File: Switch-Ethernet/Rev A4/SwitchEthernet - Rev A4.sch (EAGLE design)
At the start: 109 parts, among them J1 22-05-7028-02, J2 DF17(2.0)-20DP-0.5V(57), J3 DF17(4.0)-20DP-0.5V(57), J4 22-05-7058-05, P1 RB1-125BAG1A, T1 H1102FNL, T2 H1102FNL, U1 TC1264-3.3, U2 TC1264-1.8, U3 KSZ8995MA, U4 AT24C02C-SSHM-B, X1 NE8FAV, X2 NE8FAV, Y1 8Z-25.000MHZMAAJ-T

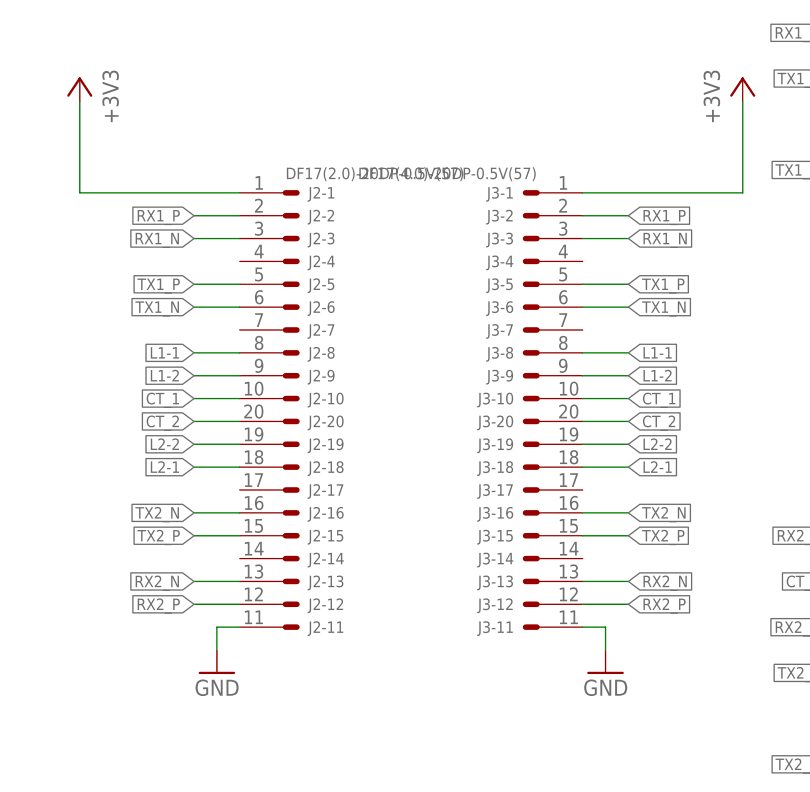
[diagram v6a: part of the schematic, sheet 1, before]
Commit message: Replace J2 to femal connector and reroute the board, replace holes
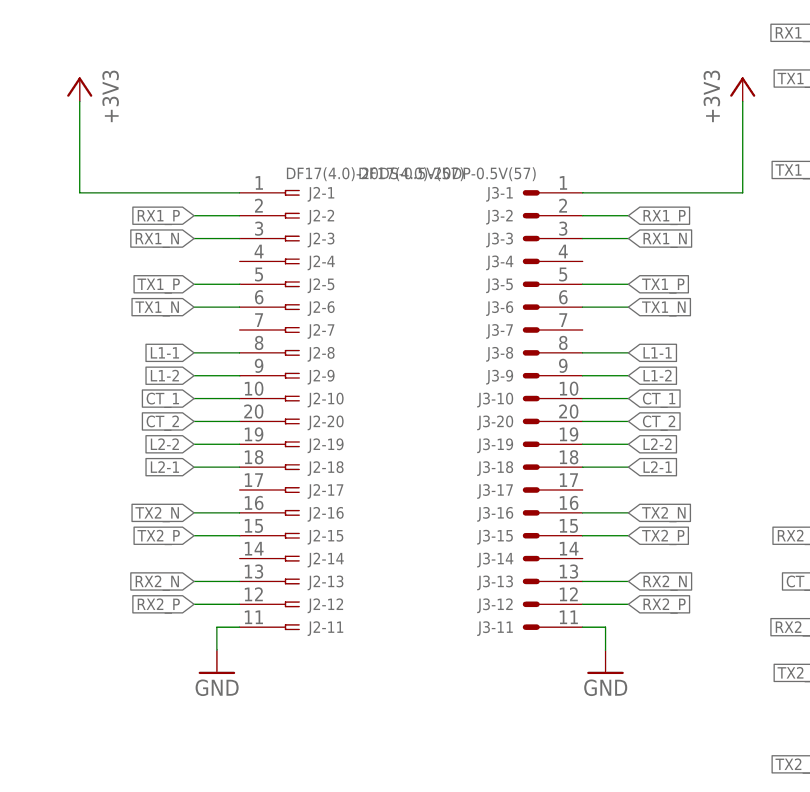
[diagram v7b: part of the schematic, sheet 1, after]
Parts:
- J2: value DF17(2.0)-20DP-0.5V(57) -> DF17(4.0)-20DS-0.5V(57); device con-hirose:DF17(2.0)-20DP-0.5V(57) -> con-hirose:DF17(4.0)-20DS-0.5V(57)
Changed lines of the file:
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@@
 <part name="+3V12" library="supply1" deviceset="+3V3" device=""/>
 <part name="+3V16" library="supply1" deviceset="+3V3" device=""/>
-<part name="J2" library="con-hirose" deviceset="DF17(?)-20DP-0.5V(57)" device="2.0"/>
+<part name="J2" library="con-hirose" deviceset="DF17(?)-20DS-0.5V(57)" device="4.0"/>
 <part name="J3" library="con-hirose" deviceset="DF17(?)-20DP-0.5V(57)" device="4.0"/>
 <part name="J4" library="con-molex" deviceset="22-?-05" device="05-7058"/>

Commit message: Modified the board according to the review
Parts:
- removed C40, C43, C44: 0.1uF, rcl:C-EUC0603
- removed C46, C47: 1000pF, 2kV, rcl:C-EUC1206
- removed J4: 22-05-7058-05, con-molex:22-05-7058-05
- removed LED7: Blue, led:LEDCHIP-LED0603
- removed R44: 1k, rcl:R-EU_R0603
- removed R45, R46: 49.9, rcl:R-EU_R0603
- removed R49: 10K, rcl:R-EU_R0603
- removed U$9: 1N4148W, diode:1N4148W
- added C25, C8: 0.1uF, rcl:C-EUC0603
- added C5, C6: 1000pF, 2kV, rcl:C-EUC1206
- added C7: 10uF, rcl:C-EUC0603
- added D1: 1N4148WS, diode:1N4148WS
- added F1: 1812L110/24DR, fuse2:1812L110/24DR
- added LED2: Blue, led:LEDCHIP-LED0603
- added MP1, MP2, MP3, MP4: MOUNT-PAD3,0, holes:MOUNT-PAD3,0
- added R1, R2, R4: 51, rcl:R-EU_R0603
- added R3: 1k5, rcl:R-EU_R0603
- added TP1, TP2, TP3, TP4, TP5: TPB1,27, testpad:TPB1,27
- C1, C2: value 1uF -> 1000pF, 2kV; device rcl:C-EUC0603 -> rcl:C-EUC1206; OC_NEWARK (none) -> 21T9879
- C10, C9: value 0.1uF -> 1uF; MF MULTICOMP -> (none); MPN MC0603B104K250CT -> (none); OC_FARNELL 1759037 -> unknown; OC_NEWARK 06R4923 -> (none)
- C11, C12: value 1000pF, 2kV -> 1uF; device rcl:C-EUC1206 -> rcl:C-EUC0603; OC_NEWARK 21T9879 -> (none)
- C13, C14, C19: value 0.1uF -> 4.7uF; device rcl:C-EUC0603 -> rcl:CPOL-EUCT3216; MF MULTICOMP -> (none); MPN MC0603B104K250CT -> (none); OC_FARNELL 1759037 -> unknown; OC_NEWARK 06R4923 -> 01M8221
- C15, C16, C17: value 4.7uF -> 0.1uF; device rcl:CPOL-EUCT3216 -> rcl:C-EUC0603; MF (none) -> MULTICOMP; MPN (none) -> MC0603B104K250CT; OC_FARNELL unknown -> 1759037; OC_NEWARK 01M8221 -> 06R4923
- C18, C20: value 10uF -> 0.1uF; MF MURATA -> MULTICOMP; MPN GRM32DR71C106KA01L -> MC0603B104K250CT; OC_FARNELL 2494299 -> 1759037; OC_NEWARK 13M5149 -> 06R4923
- C3: value 1uF -> 10uF; MF (none) -> MURATA; MPN (none) -> GRM32DR71C106KA01L; OC_FARNELL unknown -> 2494299; OC_NEWARK (none) -> 13M5149
- C4: value 1uF -> 0.1uF; MF (none) -> MULTICOMP; MPN (none) -> MC0603B104K250CT; OC_FARNELL unknown -> 1759037; OC_NEWARK (none) -> 06R4923
- R13, R6: value 75 -> 51; MPN MCMR06X75R0FTL -> MCMR06X49R9FTL; OC_FARNELL 2073571 -> 2073520; OC_NEWARK 58K4654 -> 58K4614
- R14, R15: value 51 -> 75; MPN MCMR06X49R9FTL -> MCMR06X75R0FTL; OC_FARNELL 2073520 -> 2073571; OC_NEWARK 58K4614 -> 58K4654
- R16, R17, R18: value 51 -> 1k; MPN MCMR06X49R9FTL -> MCMR06X1001FTL; OC_FARNELL 2073520 -> 2073348; OC_NEWARK 58K4614 -> 86T3505
- R19: value 49.9 -> 1k; MPN MCMR06X49R9FTL -> MCMR06X1001FTL; OC_FARNELL 2073520 -> 2073348; OC_NEWARK 79M5983 -> 86T3505
- R27: value 1k5 -> 49.9; MPN MCMR06X1501FTL -> MCMR06X49R9FTL; OC_FARNELL 2073391 -> 2073520; OC_NEWARK 58K4488 -> 79M5983
- R30, R31: value 10K, DNI -> 49.9; MF (none) -> MULTICOMP; MPN (none) -> MCMR06X49R9FTL; OC_FARNELL unknown -> 2073520; OC_NEWARK 58K4450 -> 79M5983
- R34: value 3k01 -> 10K; MPN MCMR06X3001FTL -> MCMR06X1002FTL; OC_FARNELL 2073461 -> 2073349; OC_NEWARK 94W5780 -> 58K4450
- R35: value 0, DNI -> 3k01; MF (none) -> MULTICOMP; MPN (none) -> MCMR06X3001FTL; OC_FARNELL unknown -> 2073461; OC_NEWARK 58K4684 -> 94W5780
- R36, R37: value 0, DNI -> 10K, DNI; OC_NEWARK 58K4684 -> 58K4450
- R41, R42, R43: value 1k -> 0, DNI; MF MULTICOMP -> (none); MPN MCMR06X1001FTL -> (none); OC_FARNELL 2073348 -> unknown; OC_NEWARK 86T3505 -> 58K4684
- renumbered C41 to C22, C42 to C24, C45 to C23, JP10 to JP4, JP7 to JP1, JP8 to JP2, JP9 to JP3, L3 to L1, LED6 to LED3, R47 to R28, R48 to R29, U$8 to T3, Y1 to -25.000MHZMAAJ-T1
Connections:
- new net N$2: F1.1, J1-2.S
- net +1V8: now also C12.1, C29.1, C30.1, C32.1, C33.1; no longer C3.1, C31.1, C34.1, C37.1, C40.1
- net +3V3: now also C11.1, C13.+, C14.+, C19.+, C25.1, C31.1, C34.1, C37.1, D1.1, R16.2, R17.2, R18.2, R19.2, R34.2, R36.2, R37.2; no longer C15.+, C16.+, C17.+, C2.1, C29.1, C30.1, C32.1, C43.1, R30.2, R31.2, R41.2, R42.2, R43.2, R44.2, R49.2, U$9.1
- net +5V: now also C10.1, C7.1, C8.1, C9.1, R3.2; no longer C1.1, C20.1, C21.1, C4.1, R27.2
- net AGND: now also C1.1, C2.1, MP1.1, MP2.1, MP3.1, MP4.1; no longer C46.1, C47.1
- net CT_1: now also R15.2; no longer R6.2
- net CT_2: now also J2-11.P, J3-11.P, R14.2; no longer J2-20.P, J3-20.P, R13.2
- net GND: now also C13.-, C14.-, C15.2, C16.2, C17.2, C19.-, C25.2, C5.2, C6.2, C7.2, C8.2, J2-20.P, J3-20.P, R35.1, TP5.TP; no longer C13.2, C14.2, C15.-, C16.-, C17.-, C19.2, C40.2, C43.2, C44.2, C46.2, C47.2, J2-11.P, J3-11.P, J4-5.S, R34.1
- net ISET: now also R35.2; no longer R34.2
- net L1-1: now also LED2.C; no longer LED4.C
- net L1-2: now also LED4.C; no longer LED5.C
- net L2-2: now also LED5.C; no longer LED7.C
- net N$10: now also C15.1, R22.1; no longer C9.1, R19.1
- net N$11: now also R12.2; no longer R17.2
- net N$12: now also R8.2; no longer R12.2
- net N$13: now also C5.1, R11.1, R14.1, R5.1; no longer C11.1, R13.1, R15.1, R7.1
- net N$14: now also R1.1, R6.1, R7.2; no longer R10.2, R11.1, R5.1
- net N$15: now also R2.2; no longer R16.2
- net N$16: now also R2.1, R4.1, R5.2; no longer R16.1, R7.2, R9.1
- net N$17: now also R12.1, R13.2, R9.1; no longer R17.1, R18.2, R8.1
- net N$18: now also R10.2; no longer R14.2
- net N$19: now also R10.1, R11.2, R8.1; no longer R12.1, R14.1, R15.2
- net N$20: now also LED2.A, R16.1; no longer LED4.A, R41.1
- net N$23: now also R3.1; no longer R27.1
- net N$27: now also C20.1, R30.1, R31.1; no longer C33.1, R32.1, R33.1
- net N$28: now also LED4.A, R18.1; no longer LED5.A, R42.1
- net N$29: now also R17.1; no longer R43.1
- net N$30: now also LED5.A, R19.1; no longer LED7.A, R44.1
- net N$31: now also C21.1, R32.1, R33.1; no longer C44.1, R45.1, R46.1
- net N$32: now also C6.1, R13.1, R15.1, R7.1; no longer C12.1, R10.1, R18.1, R6.1
- net N$33: now also C17.1, R24.1, R26.1; no longer C10.1, R21.1, R22.1
- net N$40: now also C16.1, R21.1; no longer C13.1, R24.1
- net N$41: now also C18.1, R27.1; no longer C14.1, R26.1
- net N$5: now also R4.2; no longer R9.2
- net N$7: now also R1.2; no longer R11.2
- net N$8: now also R6.2; no longer R5.2
- net N$9: now also R9.2; no longer R8.2
- net PS0: now also R37.1; no longer R31.1
- net PS1: now also R36.1; no longer R30.1
- net PW: now also C3.1, C4.1, F1.2; no longer C18.1, C19.1, J1-2.S
- net RST_N: now also D1.2, R34.1; no longer R49.1, U$9.2
- net RX1_ISO_N: now also R24.2; no longer R21.2
- net RX1_ISO_P: now also R26.2; no longer R22.2
- net RX2_ISO_P: now also R27.2; no longer R26.2
- net RX3_ISO_N: now also R33.2; no longer R46.2
- net RX3_ISO_P: now also R32.2; no longer R45.2
- net SCL: now also R40.1, R41.1; no longer R37.1, R38.1
- net SCL_CPU: now also R41.2, TP2.TP; no longer J4-2.S, R38.2
- net SCL_EEPROM: now also R40.2; no longer R37.2
- net SDA: now also R38.1, R39.1; no longer R35.1, R36.1
- net SDA_CPU: now also R39.2, TP3.TP; no longer J4-3.S, R36.2
- net SDA_EEPROM: now also R38.2; no longer R35.2
- net SPIQ: now also R42.1; no longer R39.1
- net SPIQ_CPU: now also R42.2, TP1.TP; no longer J4-1.S, R39.2
- net SPIS-N: now also R43.1; no longer R40.1
- net SPIS-N_CPU: now also R43.2, TP4.TP; no longer J4-4.S, R40.2
- net TX1_ISO_N: now also R20.2; no longer R19.2
- net TX1_ISO_P: now also R22.2; no longer R20.2
- net TX2_ISO_N: now also R21.2; no longer R23.2
- net TX2_ISO_P: now also R23.2; no longer R24.2
- net TX3_ISO_N: now also R31.2; no longer R33.2
- net TX3_ISO_P: now also R30.2; no longer R32.2
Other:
- moved on the sheet: C1, C10, C11, C12, C18, C2, C20, C21, C26, C27, C28, C29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
